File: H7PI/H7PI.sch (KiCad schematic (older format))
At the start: 37 parts, among them J1 XKTF-015-N, J2 Header_2x20, J3 USBC_16P_4MP, J5 Header_2x20, U1 AMS1117-3.3, U2 LY68L6400SLIT, U3 STM32H750VBT6, U4 W25Q64JVSSIQ, U5 W25Q64JVSSIQ, X1 32.768kHz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

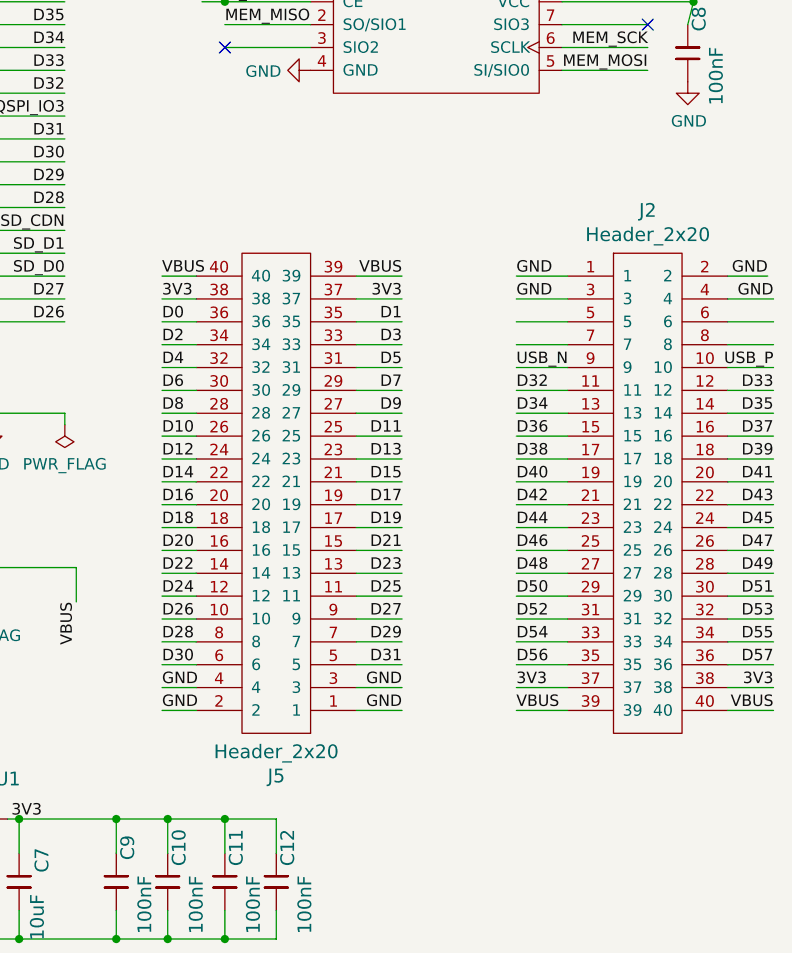
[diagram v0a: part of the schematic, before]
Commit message: v1.0第一次推送，待打样 Signed-off-by: fuhua-chen <fuhua-chen@outlook.com>
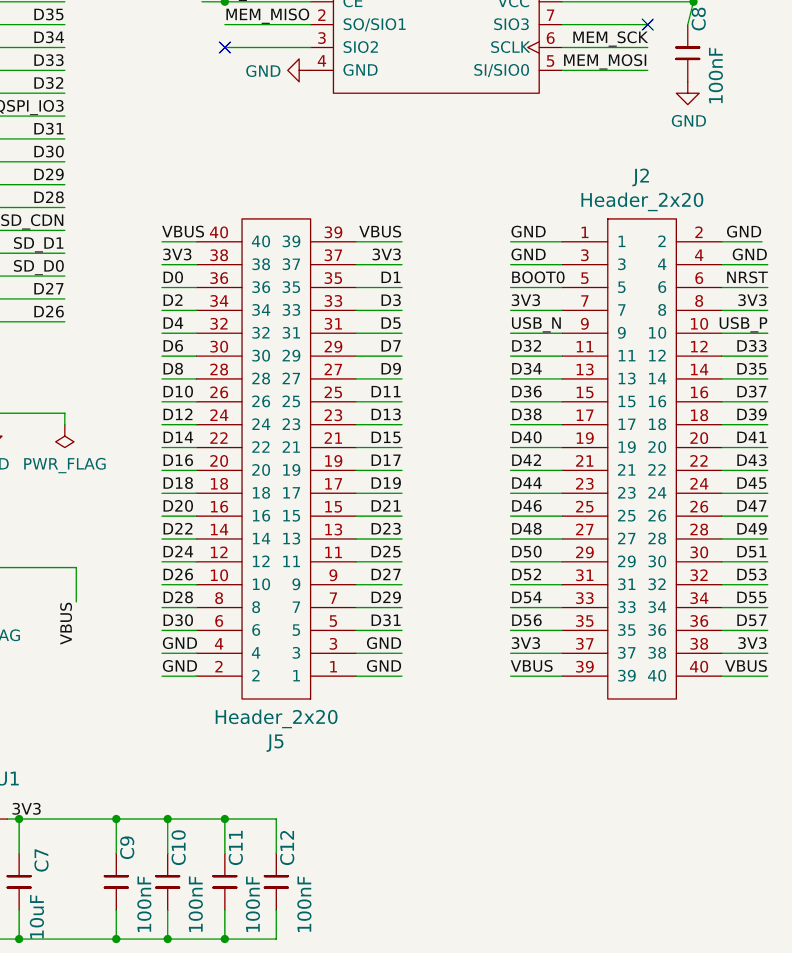
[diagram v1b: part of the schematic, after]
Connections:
- net 3V3: now also J2.7, J2.8
- net BOOT0: now also J2.5
- net NRST: now also J2.6
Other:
- moved on the sheet: J2, J5

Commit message: 更新晶振配置 Signed-off-by: fuhua.chen <fuhua-chen@outlook.com>
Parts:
- C3, C5: value 8pF -> 12pF; symbol capacitor:0402CG180J500NT -> capacitor:0402CG120J500NT; PartNumber 0402CG180J500NT -> 0402CG120J500NT; Price ￥0.006839 -> ￥0.008293; Sku C1549 -> C1547; Supplier https://item.szlcsc.com/1901.html -> https://item.szlcsc.com/1899.html
- X2: symbol crystal:S2232000082060 -> crystal:S3232000121040
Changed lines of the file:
@@
 QSPI_IO3
 $Comp
-L crystal:S2232000082060 X2
+L crystal:S3232000121040 X2
 U 1 1 5F0A57CE
 P 950 3225
@@
 $EndComp
 $Comp
-L capacitor:0402CG180J500NT C3
+L capacitor:0402CG120J500NT C3
 U 1 1 5F0A653D
 P 775 2950
 F 0 "C3" H 650 2900 60  0000 C CNN
-F 1 "8pF" H 675 2825 60  0000 C CNN
+F 1 "12pF" H 675 2825 60  0000 C CNN
 F 2 "C_0402_1005Metric" H 675 2550 60  0001 C CNN
-F 3 "https://atta.szlcsc.com/upload/public/pdf/source/20170923/C1549_1506149266585988356.pdf" H 725 2450 60  0001 C CNN
+F 3 "https://atta.szlcsc.com/upload/public/pdf/source/20170923/C1547_1506149265711988354.pdf" H 725 2450 60  0001 C CNN
 F 4 "Fenghua" H 1375 2550 50  0001 C CNN "Manufacturer"
-F 5 "0402CG180J500NT" H 925 2650 50  0001 C CNN "PartNumber"
-F 6 "https://item.szlcsc.com/1901.html" H 1025 2750 50  0001 C CNN "Supplier"
-F 7 "C1549" H 775 2850 50  0001 C CNN "Sku"
-F 8 "￥0.006839" H 775 2950 50  0001 C CNN "Price"
+F 5 "0402CG120J500NT" H 925 2650 50  0001 C CNN "PartNumber"
+F 6 "https://item.szlcsc.com/1899.html" H 1025 2750 50  0001 C CNN "Supplier"
+F 7 "C1547" H 775 2850 50  0001 C CNN "Sku"
+F 8 "￥0.008293" H 775 2950 50  0001 C CNN "Price"
 	1    775  2950
 	1    0    0    -1
@@
 	950  2950 950  3025
 $Comp
-L capacitor:0402CG180J500NT C5
+L capacitor:0402CG120J500NT C5
 U 1 1 5F0EB676
 P 775 3450
 F 0 "C5" H 650 3500 60  0000 C CNN
-F 1 "8pF" H 675 3600 60  0000 C CNN
+F 1 "12pF" H 675 3600 60  0000 C CNN
 F 2 "C_0402_1005Metric" H 675 3050 60  0001 C CNN
-F 3 "https://atta.szlcsc.com/upload/public/pdf/source/20170923/C1549_1506149266585988356.pdf" H 725 2950 60  0001 C CNN
+F 3 "https://atta.szlcsc.com/upload/public/pdf/source/20170923/C1547_1506149265711988354.pdf" H 725 2950 60  0001 C CNN
 F 4 "Fenghua" H 1375 3050 50  0001 C CNN "Manufacturer"
-F 5 "0402CG180J500NT" H 925 3150 50  0001 C CNN "PartNumber"
-F 6 "https://item.szlcsc.com/1901.html" H 1025 3250 50  0001 C CNN "Supplier"
-F 7 "C1549" H 775 3350 50  0001 C CNN "Sku"
-F 8 "￥0.006839" H 775 3450 50  0001 C CNN "Price"
+F 5 "0402CG120J500NT" H 925 3150 50  0001 C CNN "PartNumber"
+F 6 "https://item.szlcsc.com/1899.html" H 1025 3250 50  0001 C CNN "Supplier"
+F 7 "C1547" H 775 3350 50  0001 C CNN "Sku"
+F 8 "￥0.008293" H 775 3450 50  0001 C CNN "Price"
 	1    775  3450
 	1    0    0    -1
